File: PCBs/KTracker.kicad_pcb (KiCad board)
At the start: 2 copper layers, 78.5 x 20.6 mm, 65 parts, among them J1 Conn_01x02_Female, J2 Conn_01x04_Female, J3 Conn_01x02_Female, J4 Conn_01x08_Female, J5 Conn_01x02_Female, P1 USB_C_Plug_USB2.0, SW1 Option/FLASH Switch, SW2 Cali Switch, SW3 SW_SPDT MAIN POWER, U1 ME6211C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

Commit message: #auto_saved_files#
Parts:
- removed U3: MPU-6050, Sensor_Motion:InvenSense_QFN-24_4x4mm_P0.5mm

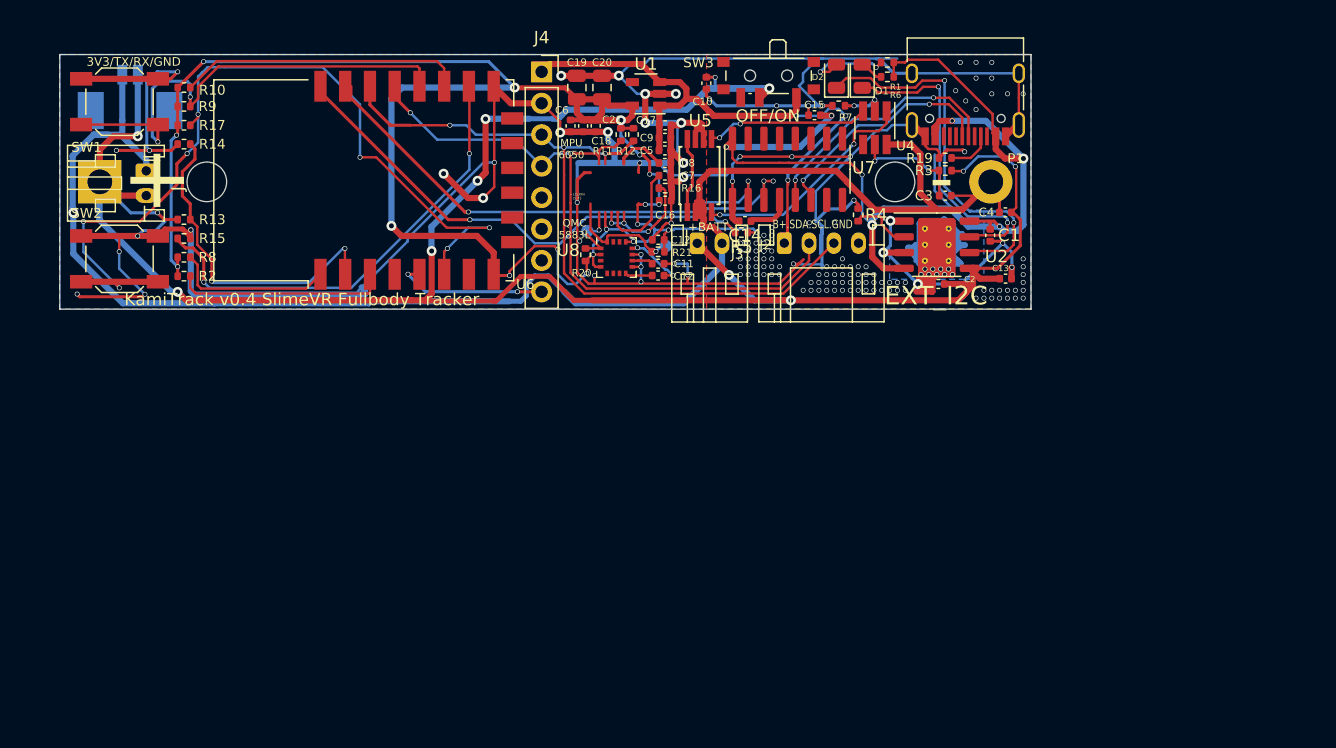
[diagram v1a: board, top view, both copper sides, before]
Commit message: MPU 6500!!
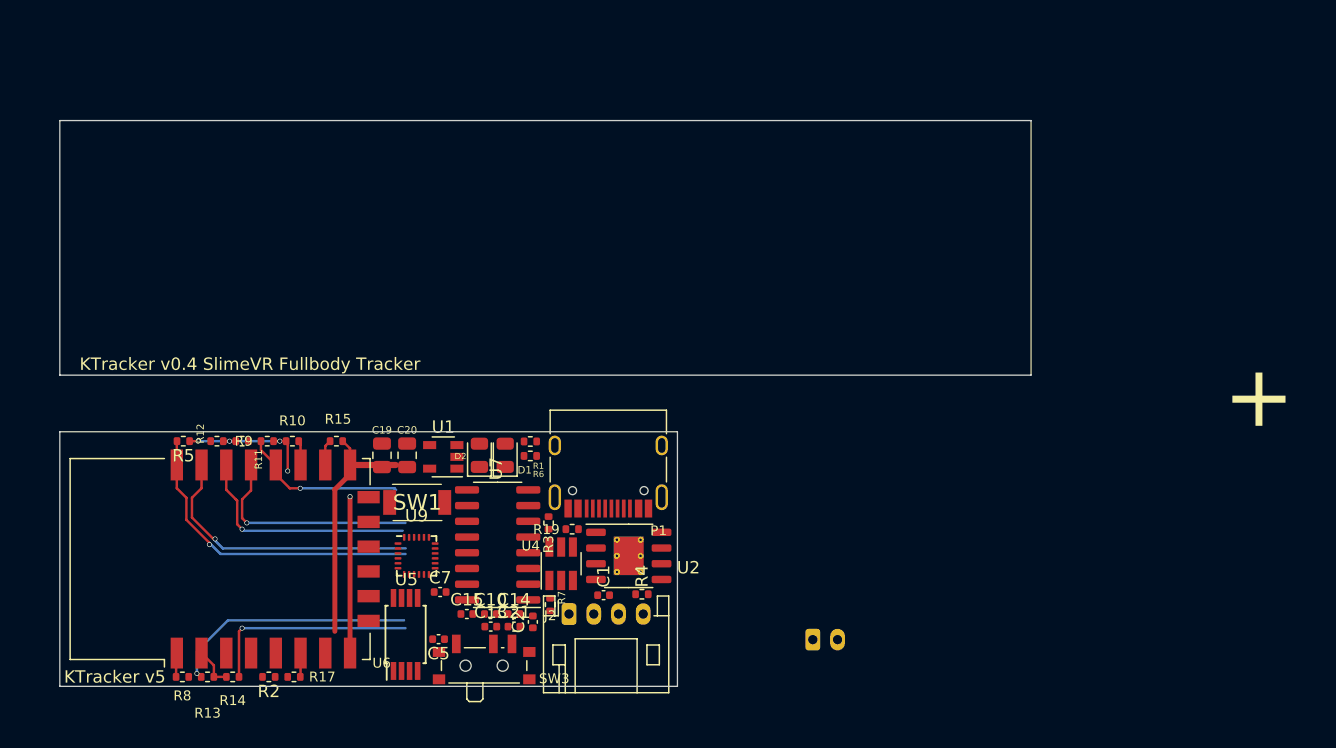
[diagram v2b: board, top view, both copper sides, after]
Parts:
- removed BT1: Battery_Cell, Battery:BatteryHolder_MPD_BH-18650-PC2
- removed C11: 4.7uF, Capacitor_SMD:C_0402_1005Metric
- removed C12: 0.22uF, Capacitor_SMD:C_0402_1005Metric
- removed C12, C16, C3: 0.1uF, Capacitor_SMD:C_0402_1005Metric
- removed C17, C18, C4, C9: 10uF, Capacitor_SMD:C_0402_1005Metric
- removed C6: 10nF, Capacitor_SMD:C_0402_1005Metric
- removed C8: 2.2nF, Capacitor_SMD:C_0402_1005Metric
- removed G***: LOGO, kami:kamilake_1100dpi
- removed J3: Conn_01x02_Female, Connector_JST:JST_PH_S2B-PH-K_1x02_P2.00mm_Horizontal
- removed J4: Conn_01x08_Female, Connector_PinSocket_2.54mm:PinSocket_1x08_P2.54mm_Vertical
- removed J5: Conn_01x02_Female, kami:MOLEX_532610271
- removed R16: 10k, Resistor_SMD:R_0402_1005Metric
- removed R20, R21: 2.2K, Resistor_SMD:R_0402_1005Metric
- removed SW2: Cali Switch, Button_Switch_SMD:SW_SPST_SKQG_WithoutStem
- removed TP1, TP2: TestPoint, TestPoint:TestPoint_Pad_D1.0mm
- removed U8: QMC5883L, Package_LGA:LGA-16_3x3mm_P0.5mm
- added U9: MPU-9250, Sensor_Motion:InvenSense_QFN-24_3x3mm_P0.4mm, F.Cu at (118.6, 95.8)
- C2: value 10uF -> 0.1uF
- J1: moved to B.Cu
- SW1: footprint Button_Switch_SMD:SW_SPST_SKQG_WithoutStem -> mod_legacy:TS-1088R
- moved J1 65.9 mm to (150.6, 102.5), turned to 0 degrees
- moved SW3 52.3 mm to (124.1, 104.3), turned to 0 degrees
- moved C13 50.2 mm to (124.6, 101.5)
- moved C15 49.1 mm to (122.7, 100.5)
- moved R5 48.2 mm to (99.8, 86.5)
- moved R7 46.6 mm to (129.4, 99.7), turned to -90 degrees
- moved C10 46.3 mm to (124.6, 100.5), turned to 0 degrees
- moved R17 45.5 mm to (108.7, 105.5)
- moved U5 44.0 mm to (117.7, 102.1)
- moved C5 43.5 mm to (120.4, 102.5), turned to 180 degrees
- moved U4 43.4 mm to (130.3, 96.4), turned to 90 degrees
- moved R14 43.1 mm to (101.7, 105.5)
- moved R3 42.9 mm to (129.3, 93.1), turned to -90 degrees
- moved C1 42.7 mm to (133.7, 98.9), turned to 0 degrees
- moved C2 42.7 mm to (128.0, 101.1), turned to 90 degrees
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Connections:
- C2 pad 1: BATT+ -> GND
- C2 pad 2: GND -> +3V3
- U6 pad 5: INT -> unconnected-(U6-Pad5)
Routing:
- net GND: track 439.6 -> 39.9 mm, vias 159 -> 1
- net BATT+: track 190.6 -> 17.2 mm, vias 12 -> 1
- net BATT-: track 134.1 -> 0.00 mm, vias 1 -> 0
- net +3V3: track 156.3 -> 24.4 mm, vias 19 -> 5
- net VBUS: track 92.9 -> 0.00 mm, vias 7 -> 0
- net Net-(R17-Pad2): track 73.5 -> 1.78 mm, vias 7 -> 0
- net VBAT: track 48.2 -> 0.00 mm, vias 3 -> 0
- net SCL: track 60.2 -> 18.7 mm, vias 3 -> 1
- net SDA: track 55.2 -> 18.0 mm, vias 2 -> 1
- net Net-(R15-Pad1): track 37.1 -> 2.09 mm, vias 2 -> 0
- net Net-(D2-Pad1): track 30.7 -> 0.00 mm, vias 2 -> 0
- net Net-(R9-Pad2): track 39.3 -> 13.4 mm, vias 2 -> 1
- net Net-(D1-Pad1): track 25.4 -> 0.00 mm, vias 2 -> 0
- net UART_ESP+: track 49.9 -> 25.7 mm, vias 4 -> 1
- net ADC: track 26.7 -> 3.35 mm, vias 2 -> 0
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- removed copper zone on B.Cu, net (none)
- removed copper zone on B.Cu, net GND
- removed copper zone on F.Cu, net GND
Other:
- board size 78.5 x 20.6 mm -> 78.5 x 45.7 mm
- board text added: "KTracker v0.4 SlimeVR Fullbody Tracker"
- board text added: "KTracker v5"
- board text removed: "+ -"
- board text removed: "+BATT-"
- board text removed: "-"
- board text removed: "3V3/TX/RX/GND"
- board text removed: "B+.SDA.SCL.GND"
- board text removed: "EXT_I2C"
- board text removed: "KamiTrack v0.4 SlimeVR Fullbody Tracker"
- board text removed: "MPU 6050"
- board text removed: "OFF/ON"
- board text removed: "QMC 5883L"
- board text removed: "~{CLKIN CUT}"

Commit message: update
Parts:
- added TP1: Batt+, Connector_Pin:Pin_D0.9mm_L10.0mm_W2.4mm_FlatFork, F.Cu at (138.4, 104.8)
- added TP2: Batt-, Connector_Pin:Pin_D0.9mm_L10.0mm_W2.4mm_FlatFork, F.Cu at (138.4, 102.0)
- U4: footprint Package_TO_SOT_SMD:SOT-23-6_Handsoldering -> Package_TO_SOT_SMD:SOT-23-6
- moved J1 16.6 mm to (134.0, 102.2), turned to -90 degrees
- moved C2 5.35 mm to (122.7, 101.5), turned to 0 degrees
- moved R7 1.89 mm to (128.0, 101.0)
- moved C1 0.64 mm to (134.4, 98.9)
- moved P1 0.13 mm to (134.0, 87.9)
- moved U4 0.10 mm to (130.4, 96.4)
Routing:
- net Net-(D2-Pad1): track 0.00 -> 22.3 mm, vias 0 -> 1
- net Net-(D1-Pad1): track 0.00 -> 19.3 mm, vias 0 -> 2
- net VBAT: track 0.00 -> 14.7 mm, vias 0 -> 1
- net GND: track 39.9 -> 53.8 mm, vias 1 -> 3
- net +3V3: track 24.4 -> 31.2 mm, vias 5 -> 7
- net Net-(D2-Pad2): track 0.00 -> 4.69 mm, vias 0 -> 2
- net Net-(R7-Pad1): track 0.00 -> 3.95 mm
- net SCL: track 18.7 -> 22.5 mm, vias 1 -> 2
- net BATT+: track 17.2 -> 20.0 mm
- net Net-(D1-Pad2): track 0.00 -> 2.46 mm
- net SDA: track 18.0 -> 19.3 mm, vias 1 -> 2

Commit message: 완성!
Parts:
- moved C21 6.23 mm to (120.5, 99.7)
- moved R19 5.83 mm to (127.8, 88.8)
- moved C2 4.45 mm to (121.1, 97.3), turned to 90 degrees
- moved TP1 1.22 mm to (137.2, 104.9)
- moved C1 0.54 mm to (134.9, 98.9)
- moved TP2 0.35 mm to (138.1, 102.1)
- moved R13 0.25 mm to (104.0, 105.5)
- moved R8 0.25 mm to (99.9, 105.5)
- moved R14 0.25 mm to (102.0, 105.5)
- moved SW3 0.13 mm to (124.1, 104.4)
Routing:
- net GND: track 53.8 -> 141.6 mm, vias 3 -> 43
- net VBUS: track 0.00 -> 54.7 mm, vias 0 -> 6
- net +3V3: track 31.2 -> 80.1 mm, vias 7 -> 13
- net BATT+: track 20.0 -> 63.3 mm, vias 1 -> 6
- net BATT-: track 0.00 -> 33.9 mm, vias 0 -> 2
- net VBAT: track 14.7 -> 44.9 mm, vias 1 -> 5
- net SDA: track 19.3 -> 40.0 mm
- net SCL: track 22.5 -> 42.2 mm, vias 2 -> 3
- net Net-(U4-Pad1): track 0.00 -> 15.1 mm, vias 0 -> 2
- net Net-(U4-Pad3): track 0.00 -> 14.3 mm, vias 0 -> 2
- net UART_ESP-: track 22.9 -> 35.1 mm, vias 1 -> 2
- net UART_ESP+: track 25.7 -> 36.4 mm, vias 1 -> 2
- net Net-(R4-Pad1): track 0.00 -> 9.10 mm, vias 0 -> 2
- net Net-(P1-PadA5): track 0.00 -> 8.80 mm
- net Net-(P1-PadA6): track 0.00 -> 8.55 mm, vias 0 -> 2
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- added copper zone on B.Cu, net GND
- added copper zone on F.Cu, net GND
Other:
- board text added: "KTracker"
- board text added: "Kamilake"
- board text added: "v0.5 es1"
- board text removed: "KTracker v5"

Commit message: !
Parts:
- removed R3: 100R, Resistor_SMD:R_0402_1005Metric
- removed R7: 1K, Resistor_SMD:R_0402_1005Metric
- removed U4: DW01, Package_TO_SOT_SMD:SOT-23-6
- removed U5: FS8205A, Package_SO:TSSOP-8_4.4x3mm_P0.65mm
- added JST-MP: JST_GH_BM02B-GHS-TBT_1x02-1MP_P1.25mm_Vertical, Connector_JST:JST_GH_BM02B-GHS-TBT_1x02-1MP_P1.25mm_Vertical, F.Cu at (136.8, 102.8)
- moved C20 21.4 mm to (131.3, 104.3), turned to 180 degrees
- moved C19 20.6 mm to (128.0, 104.3), turned to 0 degrees
- moved SW3 17.7 mm to (118.7, 87.6), turned to 180 degrees
- moved U1 15.9 mm to (128.4, 101.7)
- moved C10 13.4 mm to (137.9, 98.9)
- moved J2 13.0 mm to (117.9, 100.9)
- moved C5 11.1 mm to (131.4, 102.7)
- moved C21 9.57 mm to (129.4, 96.1), turned to 90 degrees
- moved C13 9.46 mm to (133.7, 98.9), turned to 180 degrees
- moved R4 8.00 mm to (130.3, 94.2), turned to 90 degrees
- moved C14 6.90 mm to (129.4, 94.2), turned to 90 degrees
- moved C1 5.23 mm to (130.4, 96.1), turned to 90 degrees
- moved C15 2.39 mm to (120.5, 99.4)
- moved C7 1.93 mm to (118.7, 99.4)
- moved TP1 1.37 mm to (138.6, 104.9)
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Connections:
- J1 pad 1: BATT- -> GND
- TP2 pad 1: BATT- -> GND
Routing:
- net GND: track 141.6 -> 87.2 mm, vias 43 -> 28
- net BATT-: track 33.9 -> 0.00 mm, vias 2 -> 0
- net SCL: track 42.2 -> 8.61 mm, vias 3 -> 2
- net VBUS: track 54.7 -> 26.1 mm, vias 6 -> 4
- net BATT+: track 63.3 -> 35.0 mm, vias 6 -> 3
- net Net-(D2-Pad1): track 23.6 -> 0.49 mm, vias 2 -> 1
- net SDA: track 40.0 -> 20.9 mm
- net Net-(U4-Pad1): track 15.1 -> 0.00 mm, vias 2 -> 0
- net Net-(U4-Pad3): track 14.3 -> 0.00 mm, vias 2 -> 0
- net VBAT: track 44.9 -> 35.7 mm, vias 5 -> 2
- net +3V3: track 80.1 -> 72.1 mm, vias 13 -> 12
- net Net-(R4-Pad1): track 9.10 -> 2.97 mm
- net Net-(U5-Pad1): track 5.90 -> 0.00 mm
- net Net-(C14-Pad1): track 7.41 -> 2.11 mm, vias 2 -> 0
- net UART_ESP-: track 35.1 -> 29.9 mm, vias 2 -> 1
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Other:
- board text added: "Kamilake_"
- board text added: "SlimeVR"
- board text removed: "Kamilake"

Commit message: clear silk
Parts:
- added REF**: MountingHole_2.2mm_M2_DIN965, MountingHole:MountingHole_2.2mm_M2_DIN965, F.Cu at (131.1, 68.7)
- moved C10 30.0 mm to (138.3, 69.0)
- moved C13 30.0 mm to (134.1, 69.0)
- moved C14 30.0 mm to (129.8, 64.2)
- moved C15 30.0 mm to (120.9, 69.5)
- moved C2 30.0 mm to (120.9, 68.6)
- moved C7 30.0 mm to (119.1, 69.5)
- moved J1 30.0 mm to (134.4, 72.1)
- moved R13 30.0 mm to (104.4, 75.6)
- moved R14 30.0 mm to (102.4, 75.6)
- moved R17 30.0 mm to (109.1, 75.6)
- moved R2 30.0 mm to (107.1, 75.6)
- moved R6 30.0 mm to (128.2, 57.7)
- moved R8 30.0 mm to (100.3, 75.6)
- moved U1 30.0 mm to (128.8, 71.8)
- moved R1 30.0 mm to (128.2, 56.5)
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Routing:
- net GND: track 87.2 -> 127.3 mm, vias 28 -> 31
- net SCL: track 8.61 -> 45.8 mm, vias 2 -> 4
- net +3V3: track 72.1 -> 108.9 mm, vias 12 -> 13
- net BATT+: track 35.0 -> 70.0 mm, vias 3 -> 4
- net Net-(D2-Pad1): track 0.49 -> 23.9 mm, vias 1 -> 2
- net SDA: track 20.9 -> 40.0 mm, vias 2 -> 4
- net VBAT: track 35.7 -> 51.1 mm, vias 2 -> 4
- net UART_ESP-: track 29.9 -> 35.3 mm, vias 1 -> 2
- net UART_ESP+: track 31.3 -> 36.2 mm, vias 1 -> 2
- net Net-(D2-Pad2): track 0.38 -> 4.18 mm, vias 1 -> 2
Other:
- board size 78.5 x 45.7 mm -> 49.9 x 20.6 mm
- board text added: "-"

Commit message: yay
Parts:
- turned C5 to 0 degrees
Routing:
- net GND: track 127.3 -> 154.2 mm, vias 31 -> 46
- net VBUS: track 26.1 -> 44.0 mm, vias 4 -> 6
- net VBAT: track 51.1 -> 52.5 mm
- net +3V3: track 108.9 -> 108.4 mm
- net BATT+: vias 4 -> 3

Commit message: 고로롱
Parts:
- added G***: LOGO, kamilib:kamilake_1100dpi, B.Cu at (128.6, 65.8)
- added G***: LOGO, kamilib:sleepy300dpi, B.Cu at (98.8, 68.2)
